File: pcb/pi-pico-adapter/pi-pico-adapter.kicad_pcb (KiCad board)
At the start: 2 copper layers, 33.4 x 53.4 mm, 6 parts, among them J2 RPi_GPIO

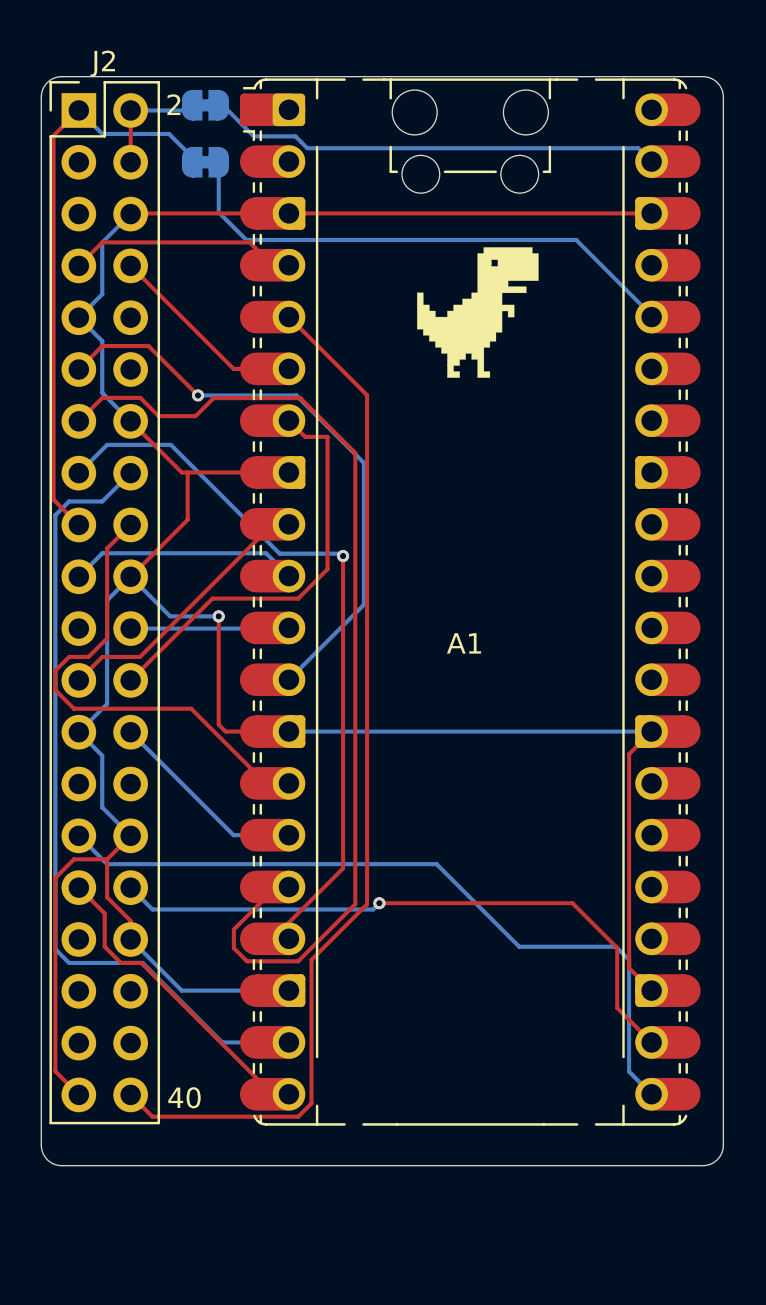
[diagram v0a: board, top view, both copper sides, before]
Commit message: feat(pcb): button input (GP18) and mounting holes
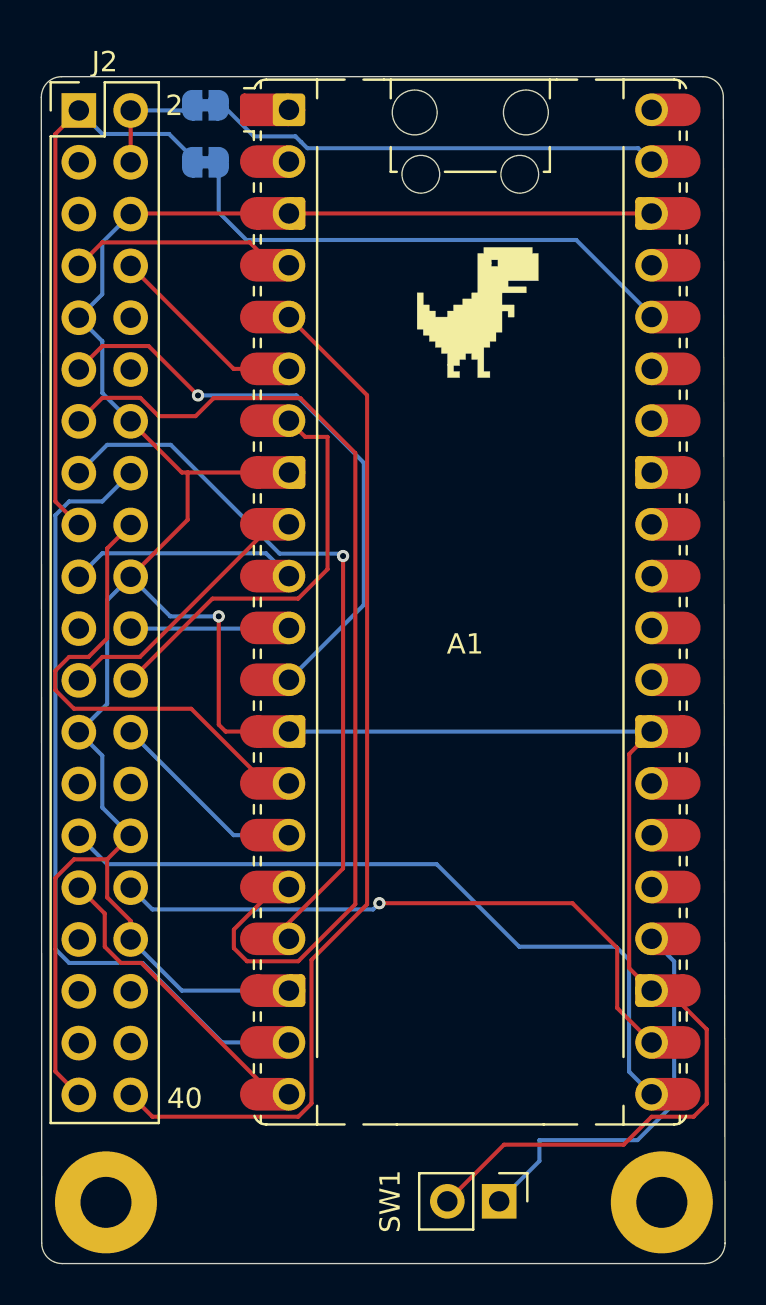
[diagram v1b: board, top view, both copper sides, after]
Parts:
- added ?: , MountingHole:MountingHole_2.5mm_Pad, F.Cu at (123.2, 134.3)
- added ?: , MountingHole:MountingHole_2.5mm_Pad, F.Cu at (150.5, 134.3)
- added SW1: SW_Push, Connector_PinHeader_2.54mm:PinHeader_1x02_P2.54mm_Vertical, F.Cu at (142.5, 134.2)
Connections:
- A1 pad 24: unconnected-(A1-GPIO18-Pad24) -> /BTN_IN
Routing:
- net GND: track 141.5 -> 162.5 mm
- net /BTN_IN: track 0.00 -> 19.7 mm
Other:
- board size 33.4 x 53.4 mm -> 33.5 x 58.2 mm
